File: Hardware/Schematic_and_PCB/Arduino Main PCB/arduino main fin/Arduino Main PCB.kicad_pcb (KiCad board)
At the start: 2 copper layers, 103.8 x 89.4 mm, 82 parts, among them J1 PIR_sensor, J10 LED_Room_2, J11 LED_Room_3, J12 LED_DOOR, J13 Buttons_Room_2, J14 Barrel_Jack, J15 Power switch, J2 Control_Panel, J3 Buttons_Room_3, J4 Buttons_Room_1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

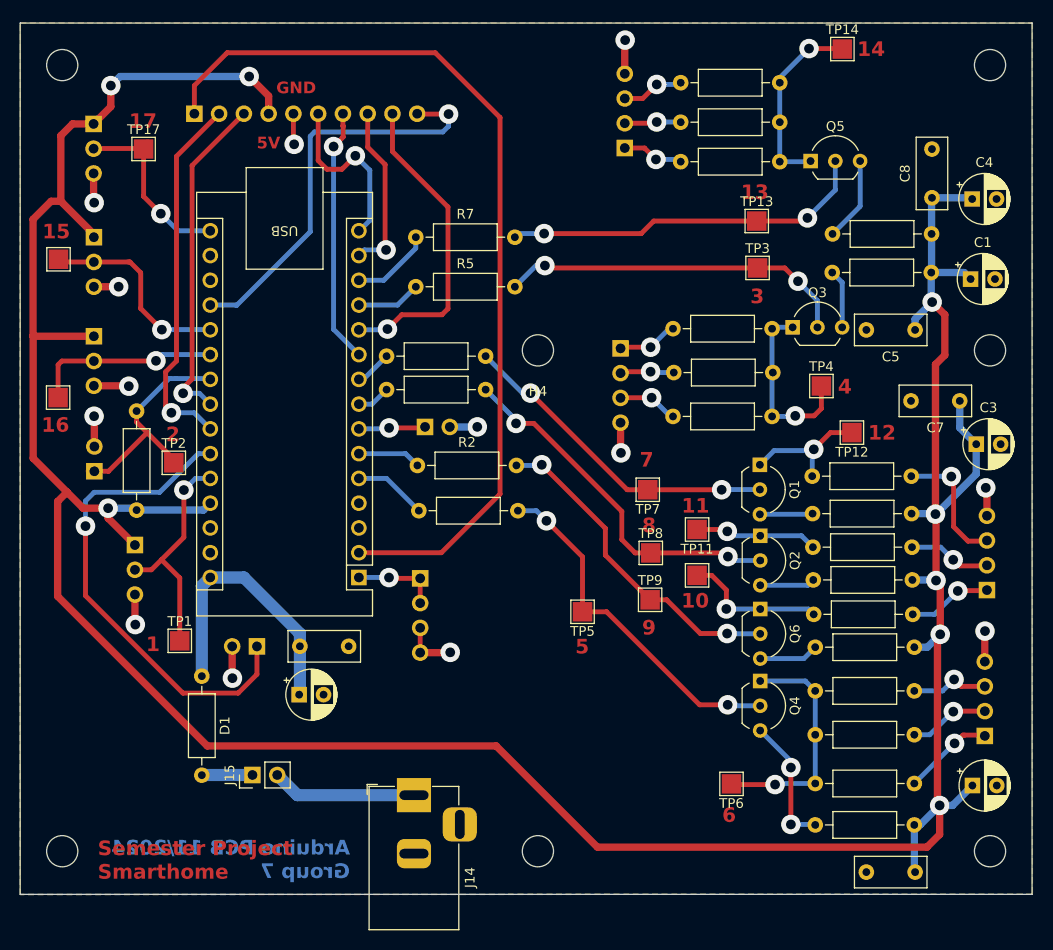
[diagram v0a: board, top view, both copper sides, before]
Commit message: created display.c
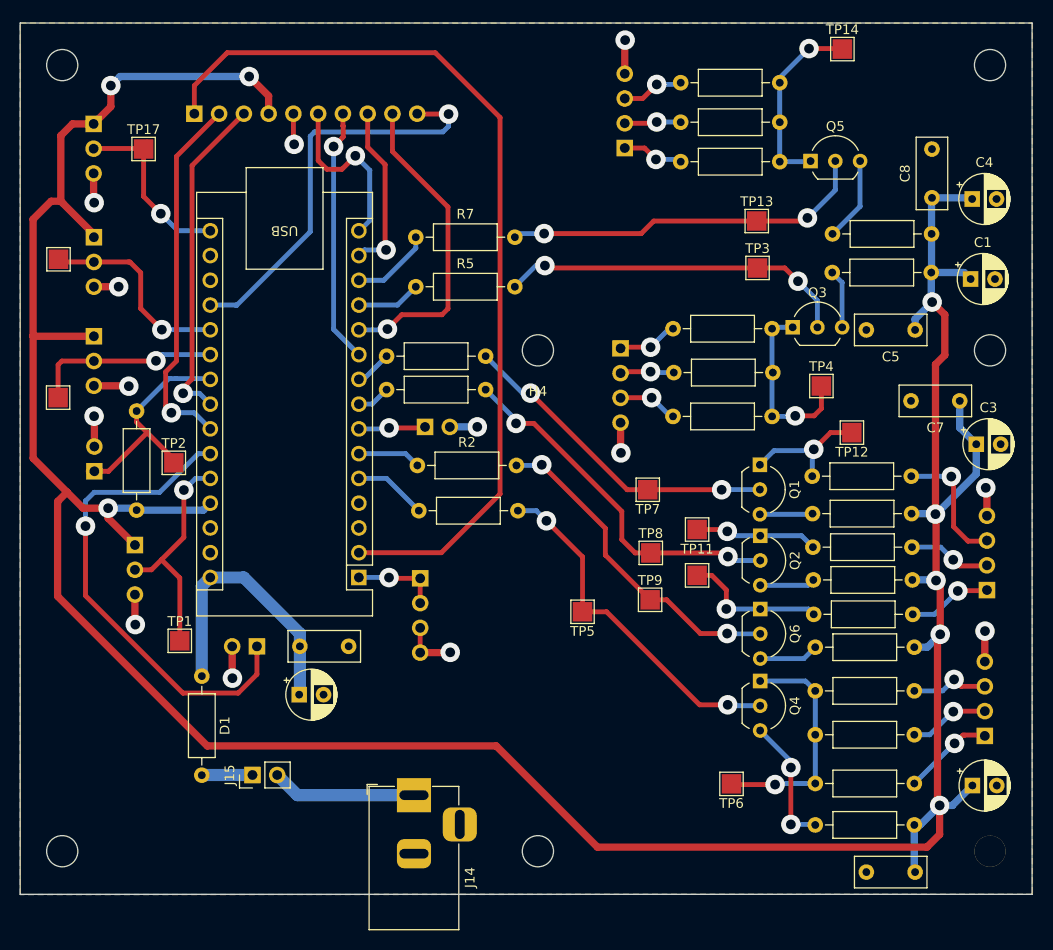
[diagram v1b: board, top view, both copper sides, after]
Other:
- board text removed: "1"
- board text removed: "10"
- board text removed: "11"
- board text removed: "12"
- board text removed: "13"
- board text removed: "14"
- board text removed: "15"
- board text removed: "16"
- board text removed: "17"
- board text removed: "2"
- board text removed: "3"
- board text removed: "4"
- board text removed: "5"
- board text removed: "5V"
- board text removed: "6"
- board text removed: "7"
- board text removed: "8"
- board text removed: "9"
- board text removed: "Arduino PCB 11/2024 Group 7"
- board text removed: "GND"
- board text removed: "Semester Project Smarthome"

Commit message: Make schematic more readable.
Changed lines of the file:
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@@
+	)
+	(gr_rect
+		(start 19.42 18.6625)
+		(end 123.21 108.0225)
+		(stroke
+			(width 0.2)
+			(type default)
+		)
+		(fill none)
+		(layer "Edge.Cuts")
 	)
 	(gr_rect
